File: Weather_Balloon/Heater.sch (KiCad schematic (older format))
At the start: 39 parts

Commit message: Logging packed
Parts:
- removed R? (x5): 4.7k, symbol R
- removed U? (x5): DS18B20, symbol DS18B20
- added C?: 22uF, symbol C
- added D?: D, symbol D
- added Q?: PSMN9R1-30YL,115, symbol Q_NMOS_GDSD
- added R?: 1k, symbol R
- added R? (x2): 18, symbol R
- added R?: 100k, symbol R
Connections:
- net +BATT: now also C?.1, D?.1 (K), R?.1, R?.1
- net GND: now also C?.2, Q?.3 (S), R?.2
- net at D?.2 (A), Q?.2 (D), Q?.4 (D): now also R?.2
- new net: Q?.1 (G), R?.1, R?.1
- new net: D?.2 (A), Q?.2 (D), Q?.4 (D), R?.2
- new net Humidity_Heat: R?.2

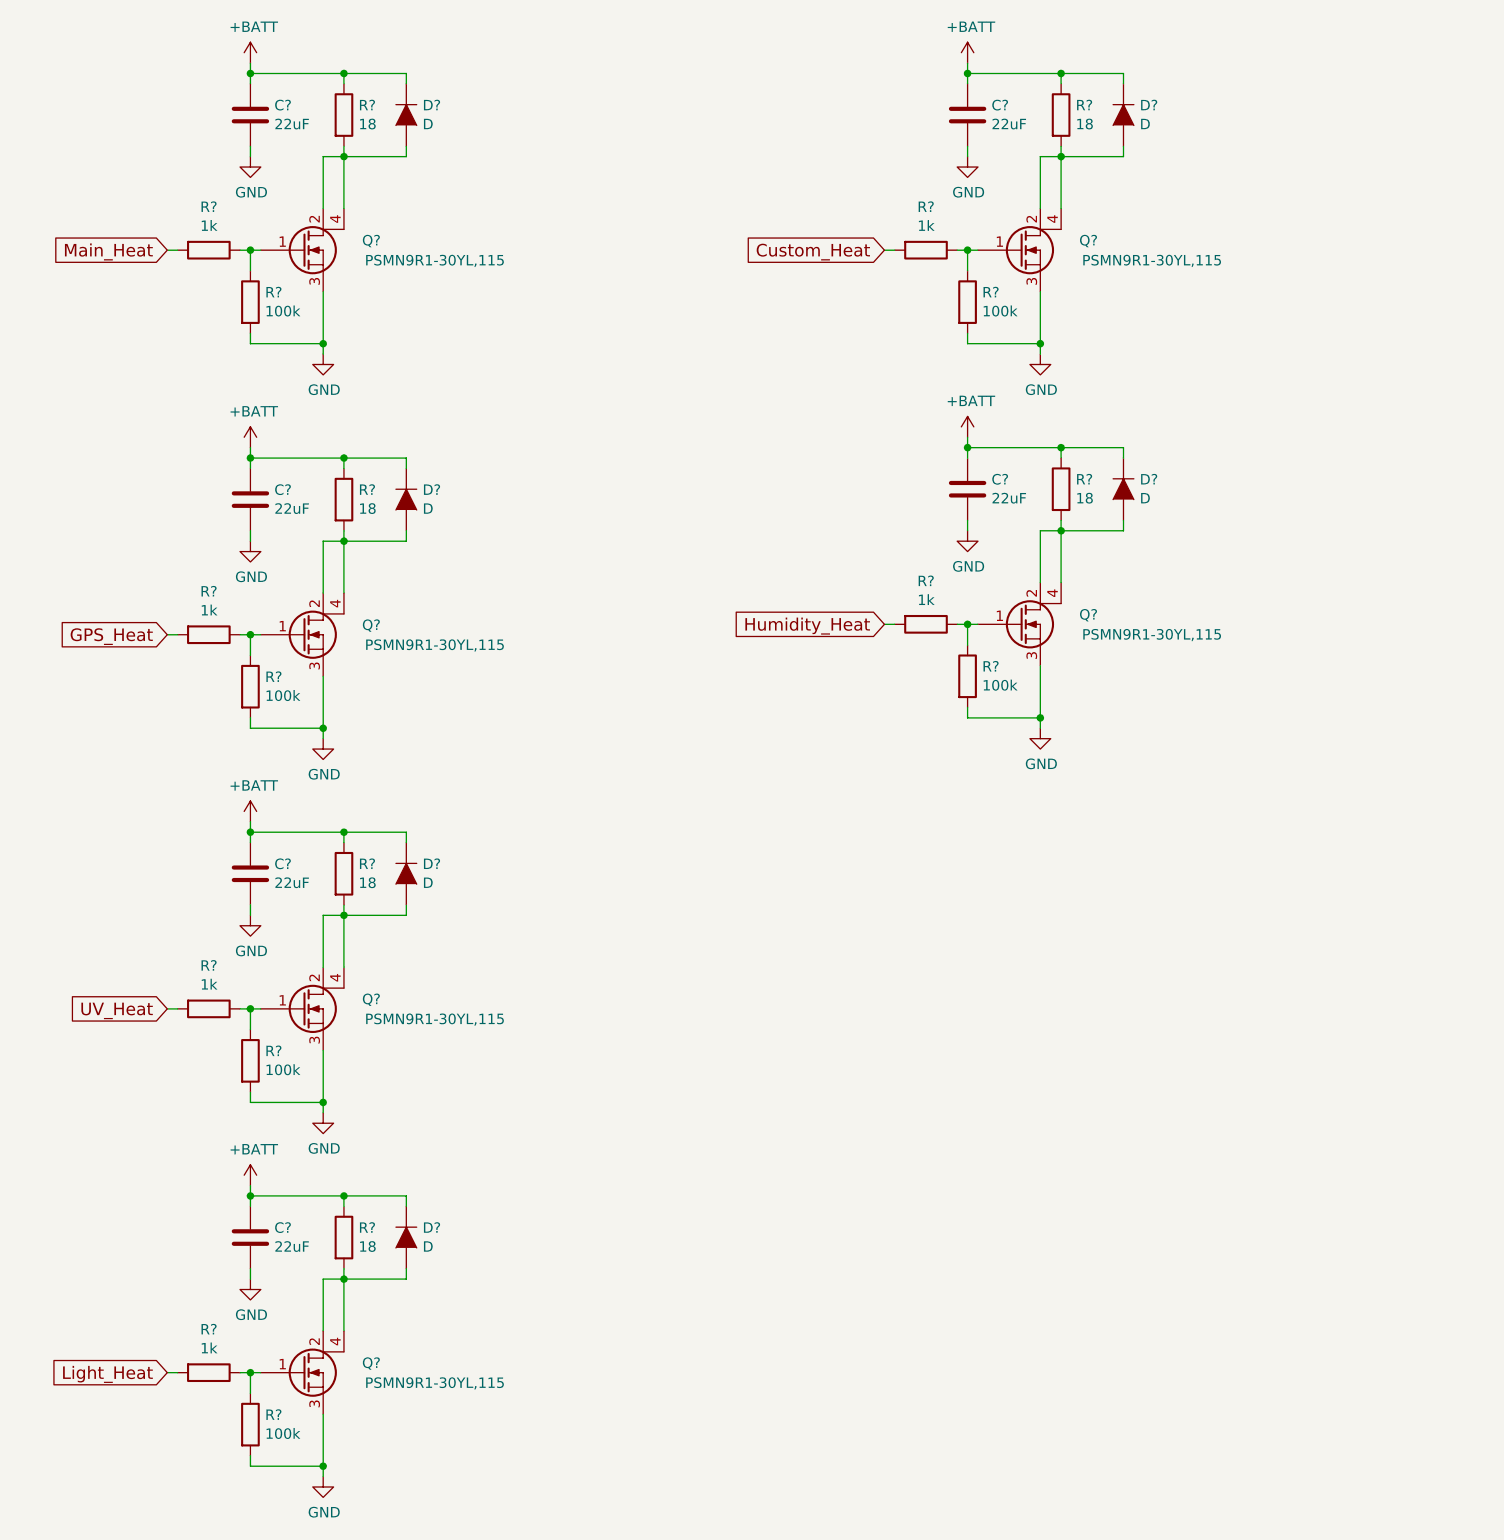
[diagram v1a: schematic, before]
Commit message: Initial PCB design with throughhole components. Layout not finilized.
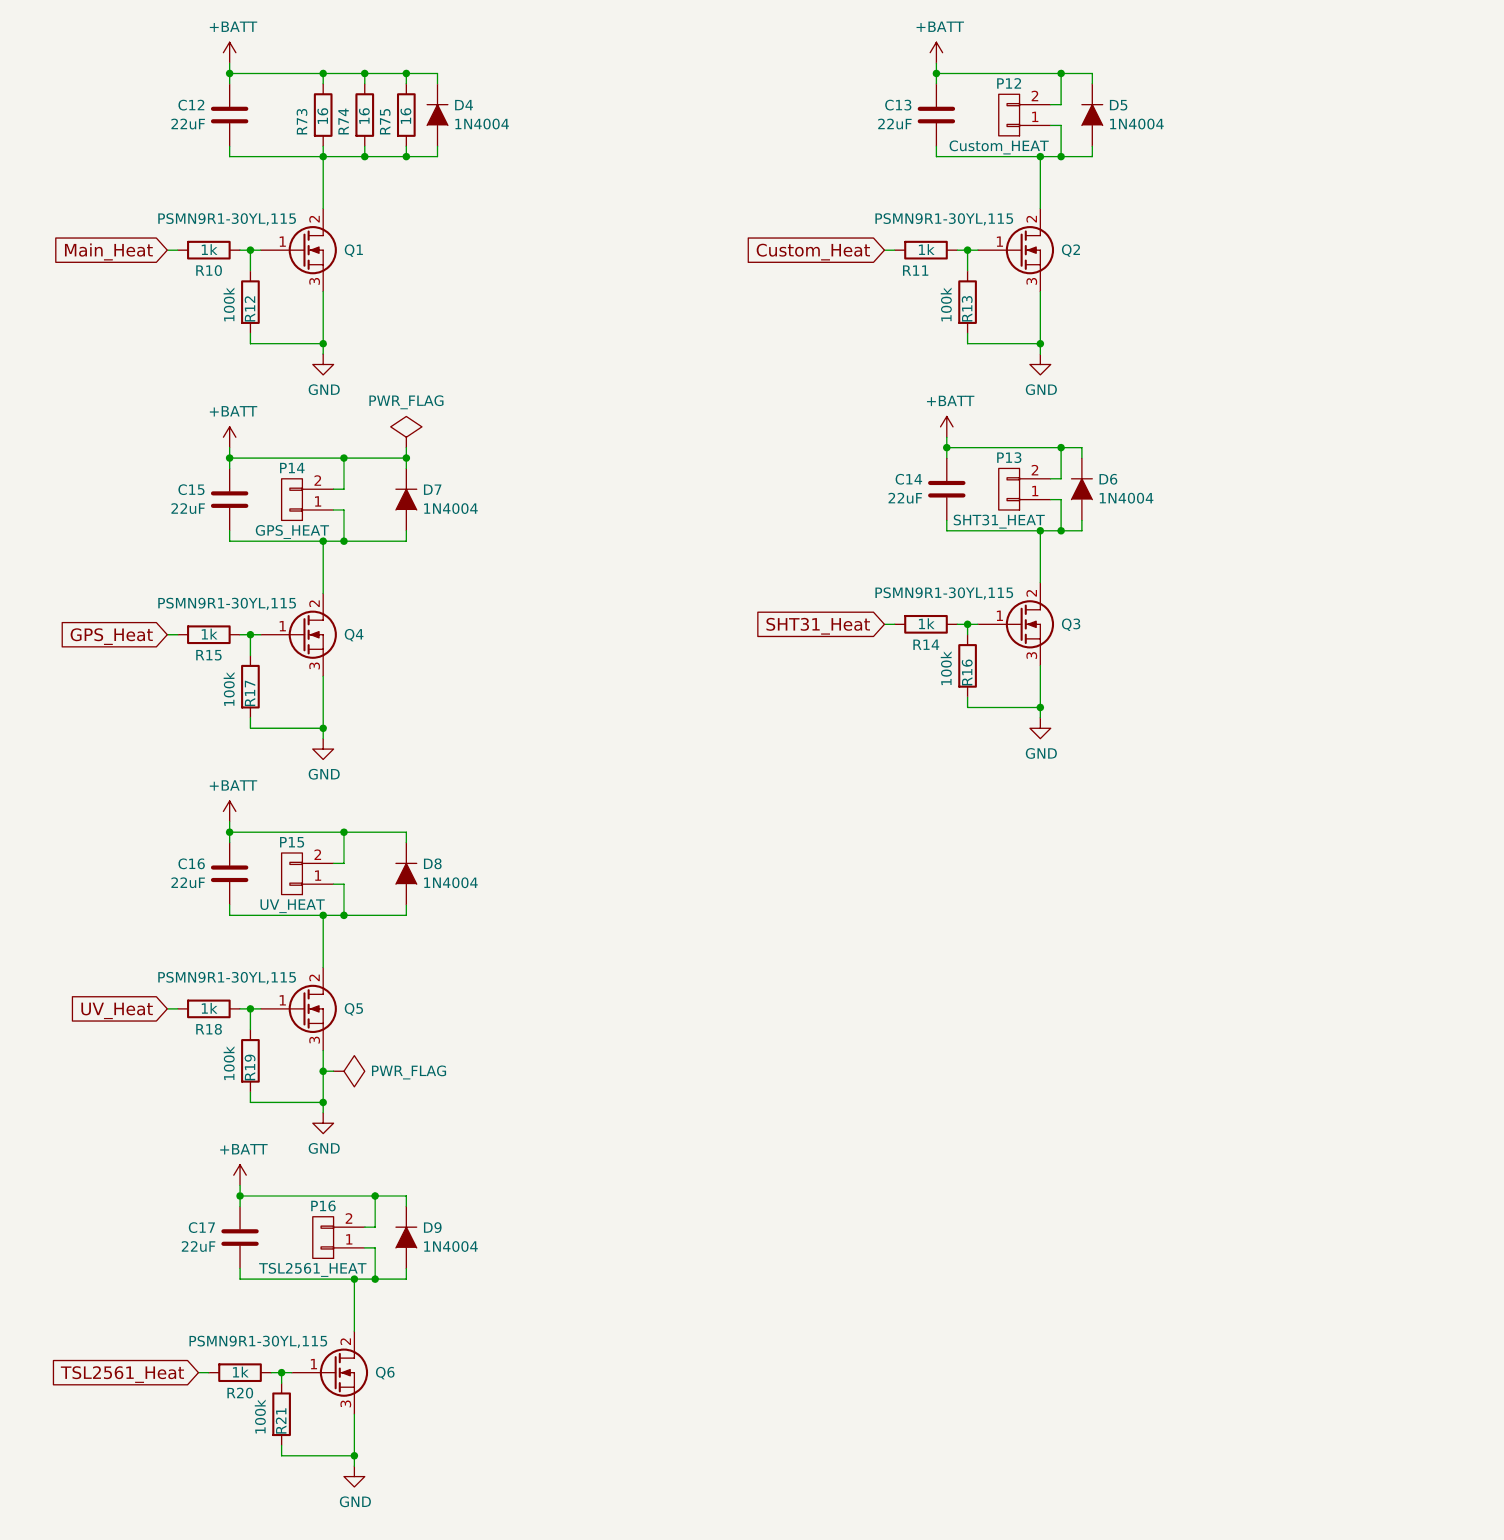
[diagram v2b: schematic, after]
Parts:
- removed D? (x6): D, symbol D
- removed Q? (x6): PSMN9R1-30YL,115, symbol Q_NMOS_GDSD
- removed R? (x6): 18, symbol R
- added D4, D5, D6, D7, D8, D9: 1N4004, Diodes_ThroughHole:Diode_DO-35_SOD27_Horizontal_RM10, symbol D
- added P12: Custom_HEAT, Personal:Pin_Header_Straight_1x02, symbol CONN_01X02
- added P13: SHT31_HEAT, Personal:Pin_Header_Straight_1x02, symbol CONN_01X02
- added P14: GPS_HEAT, Personal:Pin_Header_Straight_1x02, symbol CONN_01X02
- added P15: UV_HEAT, Personal:Pin_Header_Straight_1x02, symbol CONN_01X02
- added P16: TSL2561_HEAT, Personal:Pin_Header_Straight_1x02, symbol CONN_01X02
- added Q1, Q2, Q3, Q4, Q5, Q6: PSMN9R1-30YL,115, Personal:SOT-669_LFPAK, symbol Q_NMOS_GDS
- added R73, R74, R75: 16, Resistors_ThroughHole:Resistor_Horizontal_RM15mm, symbol R
- C12, C13, C14, C15, C16, C17: renamed from C?; footprint (none) -> Capacitors_Tantalum_SMD:TantalC_SizeC_EIA-6032_HandSoldering
- R10, R11, R12, R13, R14, R15, R16, R17, R18, R19, R20, R21: renamed from R?; footprint (none) -> Resistors_SMD:R_1206_HandSoldering
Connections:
- net +BATT: now also D4.1 (K), D5.1 (K), D6.1 (K), D7.1 (K), D8.1 (K), D9.1 (K), P12.2 (P2), P13.2 (P2), P14.2 (P2), P15.2 (P2), P16.2 (P2), R73.1, R74.1, R75.1
- net GND: now also Q1.3 (S), Q2.3 (S), Q3.3 (S), Q4.3 (S), Q5.3 (S), Q6.3 (S); no longer C12.2, C13.2, C14.2, C15.2, C16.2, C17.2
- net at R10.1, R12.1: now also Q1.1 (G)
- net at R15.1, R17.1: now also Q4.1 (G)
- net at R18.1, R19.1: now also Q5.1 (G)
- net at R20.1, R21.1: now also Q6.1 (G)
- net at R11.1, R13.1: now also Q2.1 (G)
- net at R14.1, R16.1: now also Q3.1 (G)
- net Humidity_Heat renamed SHT31_Heat
- net Light_Heat renamed TSL2561_Heat
- new net: C12.2, D4.2 (A), Q1.2 (D), R73.2, R74.2, R75.2
- new net: C15.2, D7.2 (A), P14.1 (P1), Q4.2 (D)
- new net: C16.2, D8.2 (A), P15.1 (P1), Q5.2 (D)
- new net: C17.2, D9.2 (A), P16.1 (P1), Q6.2 (D)
- new net: C13.2, D5.2 (A), P12.1 (P1), Q2.2 (D)
- new net: C14.2, D6.2 (A), P13.1 (P1), Q3.2 (D)
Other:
- moved on the sheet: C12, C13, C14, C15, C16, C17, R16, R20, R21

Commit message: Before manual trace width adjust
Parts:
- D4, D5, D6, D7, D8, D9: footprint Diodes_ThroughHole:Diode_DO-35_SOD27_Horizontal_RM10 -> Diodes_SMD:SMA_Handsoldering
- P12, P13, P14, P15, P16: footprint Personal:Pin_Header_Straight_1x02 -> Pin_Headers:Pin_Header_Straight_1x02
- R73, R74, R75: footprint Resistors_ThroughHole:Resistor_Horizontal_RM15mm -> Resistors_SMD:R_1206_HandSoldering
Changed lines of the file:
@@
 	1550 1650 1650 1650
 $Comp
-L GND #PWR027
+L GND #PWR029
 U 1 1 57DC97DF
 P 1950 2150
-F 0 "#PWR027" H 1950 1900 50  0001 C CNN
+F 0 "#PWR029" H 1950 1900 50  0001 C CNN
 F 1 "GND" H 1955 1977 50  0000 C CNN
 F 2 "" H 1950 2150 50  0000 C CNN
@@
 	1950 1850 1950 2150
 $Comp
-L +BATT #PWR028
+L +BATT #PWR030
 U 1 1 57DC97E6
 P 1500 750
-F 0 "#PWR028" H 1500 600 50  0001 C CNN
+F 0 "#PWR030" H 1500 600 50  0001 C CNN
 F 1 "+BATT" H 1515 923 50  0000 C CNN
 F 2 "" H 1500 750 50  0000 C CNN
@@
 	1550 3500 1650 3500
 $Comp
-L GND #PWR029
+L GND #PWR031
 U 1 1 57DC9830
 P 1950 4000
-F 0 "#PWR029" H 1950 3750 50  0001 C CNN
+F 0 "#PWR031" H 1950 3750 50  0001 C CNN
 F 1 "GND" H 1955 3827 50  0000 C CNN
 F 2 "" H 1950 4000 50  0000 C CNN
@@
 	1950 3700 1950 4000
 $Comp
-L +BATT #PWR030
+L +BATT #PWR032
 U 1 1 57DC9837
 P 1500 2600
-F 0 "#PWR030" H 1500 2450 50  0001 C CNN
+F 0 "#PWR032" H 1500 2450 50  0001 C CNN
 F 1 "+BATT" H 1515 2773 50  0000 C CNN
 F 2 "" H 1500 2600 50  0000 C CNN
@@
 	1550 5300 1650 5300
 $Comp
-L GND #PWR031
+L GND #PWR033
 U 1 1 57DC9881
 P 1950 5800
-F 0 "#PWR031" H 1950 5550 50  0001 C CNN
+F 0 "#PWR033" H 1950 5550 50  0001 C CNN
 F 1 "GND" H 1955 5627 50  0000 C CNN
 F 2 "" H 1950 5800 50  0000 C CNN
@@
 $EndComp
 $Comp
-L +BATT #PWR032
+L +BATT #PWR034
 U 1 1 57DC9888
 P 1500 4400
-F 0 "#PWR032" H 1500 4250 50  0001 C CNN
+F 0 "#PWR034" H 1500 4250 50  0001 C CNN
 F 1 "+BATT" H 1515 4573 50  0000 C CNN
 F 2 "" H 1500 4400 50  0000 C CNN
@@
 	1700 7050 1800 7050
 $Comp
-L GND #PWR033
+L GND #PWR035
 U 1 1 57DC98D2
 P 2100 7500
-F 0 "#PWR033" H 2100 7250 50  0001 C CNN
+F 0 "#PWR035" H 2100 7250 50  0001 C CNN
 F 1 "GND" H 2105 7327 50  0000 C CNN
 F 2 "" H 2100 7500 50  0000 C CNN
@@
 	2100 7250 2100 7500
 $Comp
-L +BATT #PWR034
+L +BATT #PWR036
 U 1 1 57DC98D9
 P 1550 6150
-F 0 "#PWR034" H 1550 6000 50  0001 C CNN
+F 0 "#PWR036" H 1550 6000 50  0001 C CNN
 F 1 "+BATT" H 1565 6323 50  0000 C CNN
 F 2 "" H 1550 6150 50  0000 C CNN
@@
 	5000 1650 5100 1650
 $Comp
-L GND #PWR035
+L GND #PWR037
 U 1 1 57DC998F
 P 5400 2150
-F 0 "#PWR035" H 5400 1900 50  0001 C CNN
+F 0 "#PWR037" H 5400 1900 50  0001 C CNN
 F 1 "GND" H 5405 1977 50  0000 C CNN
 F 2 "" H 5400 2150 50  0000 C CNN
@@
 	5400 1850 5400 2150
 $Comp
-L +BATT #PWR036
+L +BATT #PWR038
 U 1 1 57DC9996
 P 4900 750
-F 0 "#PWR036" H 4900 600 50  0001 C CNN
+F 0 "#PWR038" H 4900 600 50  0001 C CNN
 F 1 "+BATT" H 4915 923 50  0000 C CNN
 F 2 "" H 4900 750 50  0000 C CNN
@@
 	5000 3450 5100 3450
 $Comp
-L GND #PWR037
+L GND #PWR039
 U 1 1 57E774A5
 P 5400 3900
-F 0 "#PWR037" H 5400 3650 50  0001 C CNN
+F 0 "#PWR039" H 5400 3650 50  0001 C CNN
 F 1 "GND" H 5405 3727 50  0000 C CNN
 F 2 "" H 5400 3900 50  0000 C CNN
@@
 	5400 3650 5400 3900
 $Comp
-L +BATT #PWR038
+L +BATT #PWR040
 U 1 1 57E774AC
 P 4950 2550
-F 0 "#PWR038" H 4950 2400 50  0001 C CNN
+F 0 "#PWR040" H 4950 2400 50  0001 C CNN
 F 1 "+BATT" H 4965 2723 50  0000 C CNN
 F 2 "" H 4950 2550 50  0000 C CNN
@@
 F 0 "D4" V 2454 1078 50  0000 L CNN
 F 1 "1N4004" V 2545 1078 50  0000 L CNN
-F 2 "Diodes_ThroughHole:Diode_DO-35_SOD27_Horizontal_RM10" H 2500 1000 50  0001 C CNN
+F 2 "Diodes_SMD:SMA_Handsoldering" H 2500 1000 50  0001 C CNN
 F 3 "" H 2500 1000 50  0000 C CNN
 	1    2500 1000
@@
 F 0 "D8" V 2304 4728 50  0000 L CNN
 F 1 "1N4004" V 2395 4728 50  0000 L CNN
-F 2 "Diodes_ThroughHole:Diode_DO-35_SOD27_Horizontal_RM10" H 2350 4650 50  0001 C CNN
+F 2 "Diodes_SMD:SMA_Handsoldering" H 2350 4650 50  0001 C CNN
 F 3 "" H 2350 4650 50  0000 C CNN
 	1    2350 4650
@@
 F 0 "D6" V 5554 2878 50  0000 L CNN
 F 1 "1N4004" V 5645 2878 50  0000 L CNN
-F 2 "Diodes_ThroughHole:Diode_DO-35_SOD27_Horizontal_RM10" H 5600 2800 50  0001 C CNN
+F 2 "Diodes_SMD:SMA_Handsoldering" H 5600 2800 50  0001 C CNN
 F 3 "" H 5600 2800 50  0000 C CNN
 	1    5600 2800
@@
 F 0 "D5" V 5604 1078 50  0000 L CNN
 F 1 "1N4004" V 5695 1078 50  0000 L CNN
-F 2 "Diodes_ThroughHole:Diode_DO-35_SOD27_Horizontal_RM10" H 5650 1000 50  0001 C CNN
+F 2 "Diodes_SMD:SMA_Handsoldering" H 5650 1000 50  0001 C CNN
 F 3 "" H 5650 1000 50  0000 C CNN
 	1    5650 1000
@@
 F 0 "D9" V 2304 6478 50  0000 L CNN
 F 1 "1N4004" V 2395 6478 50  0000 L CNN
-F 2 "Diodes_ThroughHole:Diode_DO-35_SOD27_Horizontal_RM10" H 2350 6400 50  0001 C CNN
+F 2 "Diodes_SMD:SMA_Handsoldering" H 2350 6400 50  0001 C CNN
 F 3 "" H 2350 6400 50  0000 C CNN
 	1    2350 6400
@@
 F 0 "D7" V 2304 2928 50  0000 L CNN
 F 1 "1N4004" V 2395 2928 50  0000 L CNN
-F 2 "Diodes_ThroughHole:Diode_DO-35_SOD27_Horizontal_RM10" H 2350 2850 50  0001 C CNN
+F 2 "Diodes_SMD:SMA_Handsoldering" H 2350 2850 50  0001 C CNN
 F 3 "" H 2350 2850 50  0000 C CNN
 	1    2350 2850
@@
 $EndComp
 $Comp
-L PWR_FLAG #FLG039
+L PWR_FLAG #FLG041
 U 1 1 57EB9BAB
 P 2350 2600
-F 0 "#FLG039" H 2350 2695 50  0001 C CNN
+F 0 "#FLG041" H 2350 2695 50  0001 C CNN
 F 1 "PWR_FLAG" H 2350 2824 50  0000 C CNN
 F 2 "" H 2350 2600 50  0000 C CNN
@@
 F 0 "P14" H 1800 2700 50  0000 C CNN
 F 1 "GPS_HEAT" H 1800 3000 50  0000 C CNN
-F 2 "Personal:Pin_Header_Straight_1x02" H 1800 2850 50  0001 C CNN
+F 2 "Pin_Headers:Pin_Header_Straight_1x02" H 1800 2850 50  0001 C CNN
 F 3 "" H 1800 2850 50  0000 C CNN
 	1    1800 2850
@@
 F 0 "P15" H 1800 4500 50  0000 C CNN
 F 1 "UV_HEAT" H 1800 4800 50  0000 C CNN
-F 2 "Personal:Pin_Header_Straight_1x02" H 1800 4650 50  0001 C CNN
+F 2 "Pin_Headers:Pin_Header_Straight_1x02" H 1800 4650 50  0001 C CNN
 F 3 "" H 1800 4650 50  0000 C CNN
 	1    1800 4650
@@
 F 0 "P16" H 1950 6250 50  0000 C CNN
 F 1 "TSL2561_HEAT" H 2000 6550 50  0000 C CNN
-F 2 "Personal:Pin_Header_Straight_1x02" H 1950 6400 50  0001 C CNN
+F 2 "Pin_Headers:Pin_Header_Straight_1x02" H 1950 6400 50  0001 C CNN
 F 3 "" H 1950 6400 50  0000 C CNN
 	1    1950 6400
@@
 F 0 "P12" H 5250 850 50  0000 C CNN
 F 1 "Custom_HEAT" H 5300 1150 50  0000 C CNN
-F 2 "Personal:Pin_Header_Straight_1x02" H 5250 1000 50  0001 C CNN
+F 2 "Pin_Headers:Pin_Header_Straight_1x02" H 5250 1000 50  0001 C CNN
 F 3 "" H 5250 1000 50  0000 C CNN
 	1    5250 1000
@@
 F 0 "P13" H 5250 2650 50  0000 C CNN
 F 1 "SHT31_HEAT" H 5300 2950 50  0000 C CNN
-F 2 "Personal:Pin_Header_Straight_1x02" H 5250 2800 50  0001 C CNN
+F 2 "Pin_Headers:Pin_Header_Straight_1x02" H 5250 2800 50  0001 C CNN
 F 3 "" H 5250 2800 50  0000 C CNN
 	1    5250 2800
@@
 Connection ~ 1950 5750
 $Comp
-L PWR_FLAG #FLG040
+L PWR_FLAG #FLG042
 U 1 1 57EC1E13
 P 2000 5600
-F 0 "#FLG040" H 2000 5695 50  0001 C CNN
+F 0 "#FLG042" H 2000 5695 50  0001 C CNN
 F 1 "PWR_FLAG" V 2000 5778 50  0000 L CNN
 F 2 "" H 2000 5600 50  0000 C CNN
@@
 F 0 "R73" V 1850 900 50  0000 L CNN
 F 1 "16" V 1950 950 50  0000 L CNN
-F 2 "Resistors_ThroughHole:Resistor_Horizontal_RM15mm" V 1880 1000 50  0001 C CNN
+F 2 "Resistors_SMD:R_1206_HandSoldering" V 1880 1000 50  0001 C CNN
 F 3 "" H 1950 1000 50  0000 C CNN
 	1    1950 1000
@@
 F 0 "R74" V 2050 900 50  0000 L CNN
 F 1 "16" V 2150 950 50  0000 L CNN
-F 2 "Resistors_ThroughHole:Resistor_Horizontal_RM15mm" V 2080 1000 50  0001 C CNN
+F 2 "Resistors_SMD:R_1206_HandSoldering" V 2080 1000 50  0001 C CNN
 F 3 "" H 2150 1000 50  0000 C CNN
 	1    2150 1000
@@
 F 0 "R75" V 2250 900 50  0000 L CNN
 F 1 "16" V 2350 950 50  0000 L CNN
-F 2 "Resistors_ThroughHole:Resistor_Horizontal_RM15mm" V 2280 1000 50  0001 C CNN
+F 2 "Resistors_SMD:R_1206_HandSoldering" V 2280 1000 50  0001 C CNN
 F 3 "" H 2350 1000 50  0000 C CNN
 	1    2350 1000
